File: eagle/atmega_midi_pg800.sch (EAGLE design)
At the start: 39 parts, among them IC1 78L05Z, IC2 4067N, IC3 4067N, IC4 4067N, Q1 16.000Mhz, U1 6N138, U2 ATMEGA328P_PDIP, X1 MAB6H

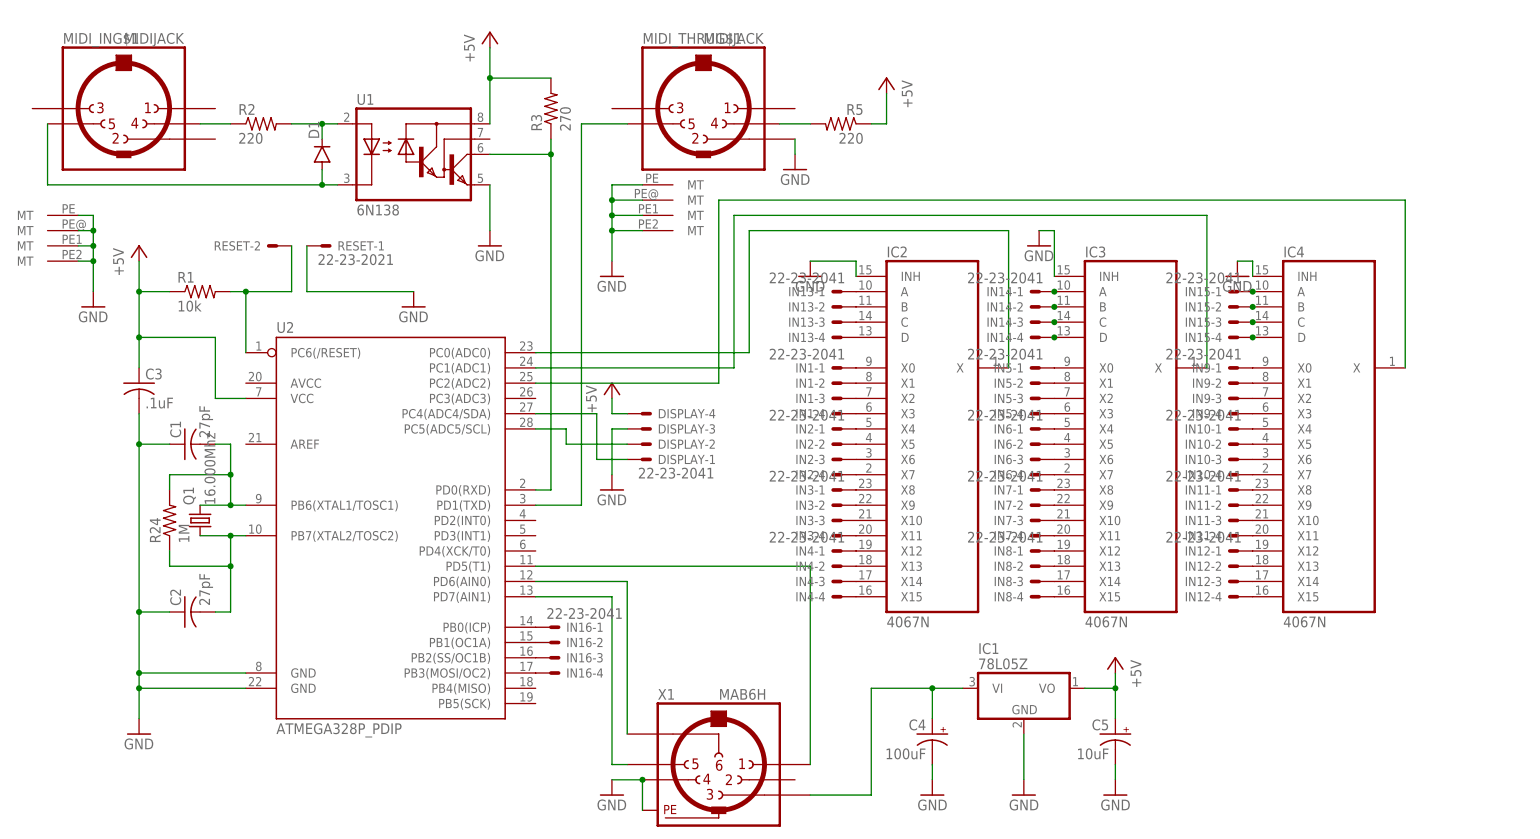
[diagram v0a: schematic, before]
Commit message: rotary encoder connection
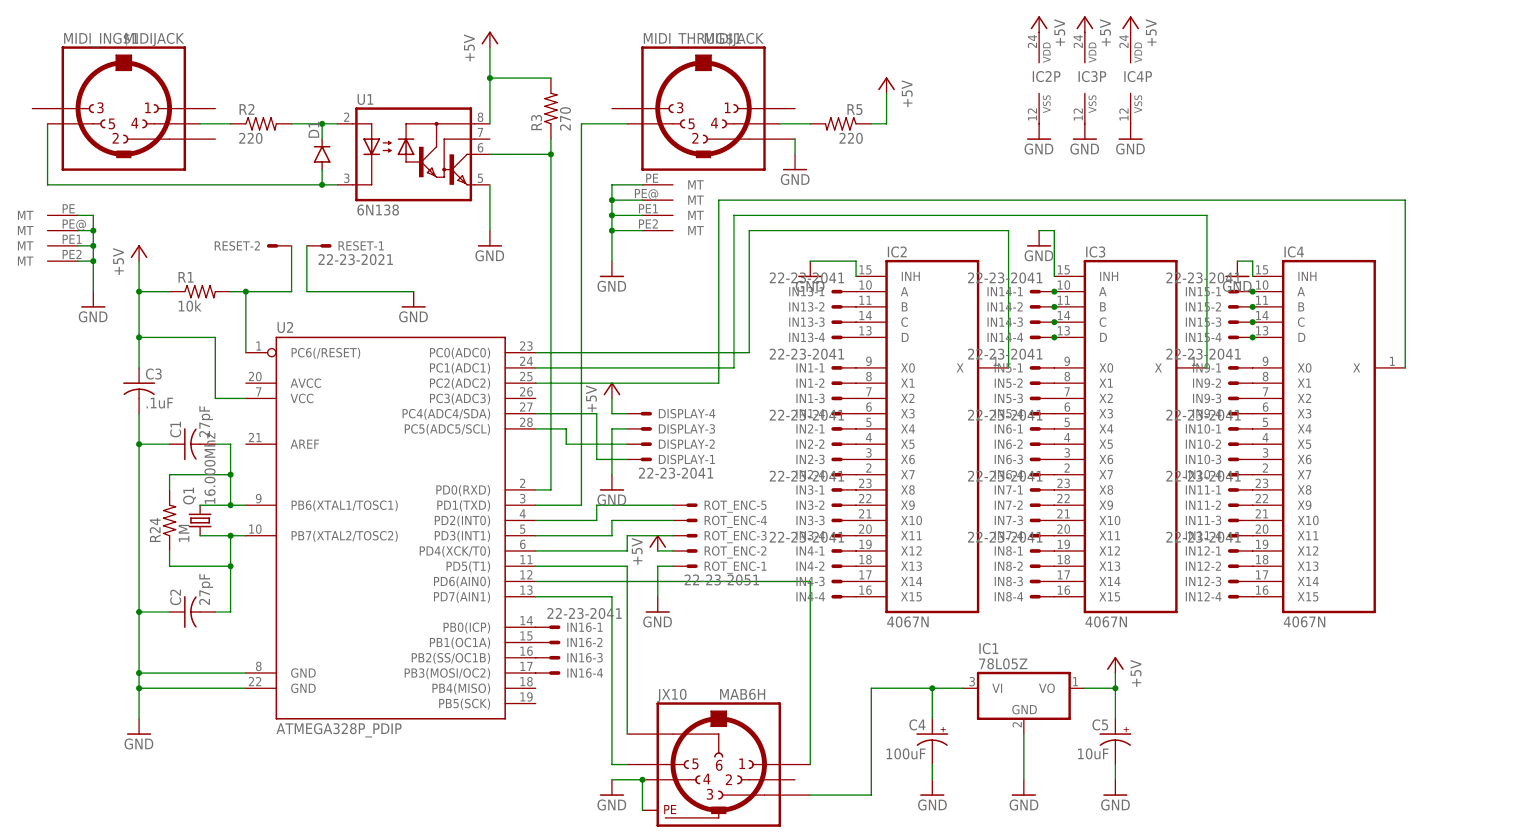
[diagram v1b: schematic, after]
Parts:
- added ROT_ENC: 22-23-2051, con-molex:22-23-2051
- R5: device rcl:R-US_0207/10 -> rcl:R-US_0309/10
- renumbered X1 to JX10
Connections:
- new net N$84: ROT_ENC-5.S, U2.PD2(INT0)
- new net N$85: ROT_ENC-4.S, U2.PD3(INT1)
- new net N$86: ROT_ENC-3.S, U2.PD4(XCK/T0)
- net +5V: now also IC2P.VDD, IC3P.VDD, IC4P.VDD, ROT_ENC-2.S
- net GND: now also IC2P.VSS, IC3P.VSS, IC4P.VSS, ROT_ENC-1.S
- net N$10: now also U2.PD6(AIN0); no longer U2.PD5(T1)
- net N$9: now also U2.PD5(T1); no longer U2.PD6(AIN0)

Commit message: big boy version of 7805 to power those 4067 and the display
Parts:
- removed IC1: 78L05Z, linear:78L05Z
- added IC5: 7805TV, linear:7805TV
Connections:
- net +5V: now also IC5.VO; no longer IC1.VO
- net GND: now also IC5.GND; no longer IC1.GND
- net N$6: now also IC5.VI; no longer IC1.VI
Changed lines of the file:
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@@
 <part name="GND1" library="supply1" deviceset="GND" device=""/>
 <part name="JX10" library="con-hirschmann" deviceset="MAB6H" device=""/>
-<part name="IC1" library="linear" deviceset="78*" device="Z" technology="L05"/>
 <part name="GND3" library="supply1" deviceset="GND" device=""/>
 <part name="C4" library="rcl" deviceset="CPOL-US" device="B45181A" value="100uF"/>
@@
 <part name="GND18" library="supply1" deviceset="GND" device=""/>
 <part name="P+9" library="supply1" deviceset="+5V" device=""/>
+<part name="IC5" library="linear" deviceset="78*" device="TV" technology="05"/>
 </parts>
 <sheets>
@@
 <instance part="GND1" gate="1" x="53.34" y="86.36"/>
 <instance part="JX10" gate="G$1" x="71.12" y="5.08"/>
-<instance part="IC1" gate="A1" x="121.92" y="17.78"/>
 <instance part="GND3" gate="1" x="53.34" y="0"/>
 <instance part="C4" gate="G$1" x="106.68" y="10.16" rot="MR0"/>
@@
 <instance part="GND18" gate="1" x="60.96" y="30.48"/>
 <instance part="P+9" gate="1" x="60.96" y="43.18"/>
+<instance part="IC5" gate="A1" x="121.92" y="17.78"/>
 </instances>
 <busses>
@@
 </segment>
 <segment>
-<pinref part="IC1" gate="A1" pin="VO"/>
 <pinref part="C5" gate="G$1" pin="+"/>
 <wire x1="132.08" y1="17.78" x2="137.16" y2="17.78" width="0.1524" layer="91"/>
@@
 <wire x1="137.16" y1="20.32" x2="137.16" y2="17.78" width="0.1524" layer="91"/>
 <junction x="137.16" y="17.78"/>
+<pinref part="IC5" gate="A1" pin="VO"/>
 </segment>
 <segment>
@@
 </segment>
 <segment>
-<pinref part="IC1" gate="A1" pin="GND"/>
 <wire x1="121.92" y1="2.54" x2="121.92" y2="10.16" width="0.1524" layer="91"/>
 <pinref part="GND15" gate="1" pin="GND"/>
+<pinref part="IC5" gate="A1" pin="GND"/>
 </segment>
 <segment>
@@
 <net name="N$6" class="0">
 <segment>
-<pinref part="IC1" gate="A1" pin="VI"/>
 <pinref part="C4" gate="G$1" pin="+"/>
 <wire x1="106.68" y1="17.78" x2="111.76" y2="17.78" width="0.1524" layer="91"/>
@@
 <wire x1="96.52" y1="17.78" x2="96.52" y2="0" width="0.1524" layer="91"/>
 <wire x1="96.52" y1="0" x2="86.36" y2="0" width="0.1524" layer="91"/>
-</segment>
-</net>
+<pinref part="IC5" gate="A1" pin="VI"/>
+</segment>
+</net>

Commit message: protectoin diode and pot power hookups
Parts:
- added D2: 1N4004, diode:1N4004
- added POT_PWR, POT_PWR1, POT_PWR2: 22-23-2021, con-molex:22-23-2021
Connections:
- net +5V: now also D2.A, POT_PWR-2.S, POT_PWR1-2.S, POT_PWR2-2.S
- net GND: now also POT_PWR-1.S, POT_PWR1-1.S, POT_PWR2-1.S
- net N$6: now also D2.C
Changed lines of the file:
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@@
 <?xml version="1.0" encoding="utf-8"?>
 <!DOCTYPE eagle SYSTEM "eagle.dtd">
-<eagle version="7.6.0">
+<eagle version="7.7.0">
 <drawing>
 <settings>
@@
 <grid distance="0.1" unitdist="inch" unit="inch" style="lines" multiple="1" display="no" altdistance="0.01" altunitdist="inch" altunit="inch"/>
 <layers>
-<layer number="1" name="Top" color="4" fill="1" visible="yes" active="no"/>
-<layer number="16" name="Bottom" color="1" fill="1" visible="yes" active="no"/>
-<layer number="17" name="Pads" color="2" fill="1" visible="yes" active="no"/>
-<layer number="18" name="Vias" color="2" fill="1" visible="yes" active="no"/>
-<layer number="19" name="Unrouted" color="6" fill="1" visible="yes" active="no"/>
-<layer number="20" name="Dimension" color="15" fill="1" visible="yes" active="no"/>
-<layer number="21" name="tPlace" color="7" fill="1" visible="yes" active="no"/>
-<layer number="22" name="bPlace" color="7" fill="1" visible="yes" active="no"/>
-<layer number="23" name="tOrigins" color="15" fill="1" visible="yes" active="no"/>
-<layer number="24" name="bOrigins" color="15" fill="1" visible="yes" active="no"/>
-<layer number="25" name="tNames" color="7" fill="1" visible="yes" active="no"/>
-<layer number="26" name="bNames" color="7" fill="1" visible="yes" active="no"/>
-<layer number="27" name="tValues" color="7" fill="1" visible="yes" active="no"/>
-<layer number="28" name="bValues" color="7" fill="1" visible="yes" active="no"/>
+<layer number="1" name="Top" color="4" fill="1" visible="no" active="no"/>
+<layer number="16" name="Bottom" color="1" fill="1" visible="no" active="no"/>
+<layer number="17" name="Pads" color="2" fill="1" visible="no" active="no"/>
+<layer number="18" name="Vias" color="2" fill="1" visible="no" active="no"/>
+<layer number="19" name="Unrouted" color="6" fill="1" visible="no" active="no"/>
+<layer number="20" name="Dimension" color="15" fill="1" visible="no" active="no"/>
+<layer number="21" name="tPlace" color="7" fill="1" visible="no" active="no"/>
+<layer number="22" name="bPlace" color="7" fill="1" visible="no" active="no"/>
+<layer number="23" name="tOrigins" color="15" fill="1" visible="no" active="no"/>
+<layer number="24" name="bOrigins" color="15" fill="1" visible="no" active="no"/>
+<layer number="25" name="tNames" color="7" fill="1" visible="no" active="no"/>
+<layer number="26" name="bNames" color="7" fill="1" visible="no" active="no"/>
+<layer number="27" name="tValues" color="7" fill="1" visible="no" active="no"/>
+<layer number="28" name="bValues" color="7" fill="1" visible="no" active="no"/>
 <layer number="29" name="tStop" color="7" fill="3" visible="no" active="no"/>
 <layer number="30" name="bStop" color="7" fill="6" visible="no" active="no"/>
@@
 <layer number="35" name="tGlue" color="7" fill="4" visible="no" active="no"/>
 <layer number="36" name="bGlue" color="7" fill="5" visible="no" active="no"/>
-<layer number="37" name="tTest" color="7" fill="1" visible="yes" active="no"/>
-<layer number="38" name="bTest" color="7" fill="1" visible="yes" active="no"/>
+<layer number="37" name="tTest" color="7" fill="1" visible="no" active="no"/>
+<layer number="38" name="bTest" color="7" fill="1" visible="no" active="no"/>
 <layer number="39" name="tKeepout" color="4" fill="11" visible="no" active="no"/>
 <layer number="40" name="bKeepout" color="1" fill="11" visible="no" active="no"/>
@@
 <layer number="44" name="Drills" color="7" fill="1" visible="no" active="no"/>
 <layer number="45" name="Holes" color="7" fill="1" visible="no" active="no"/>
-<layer number="46" name="Milling" color="3" fill="1" visible="yes" active="no"/>
-<layer number="47" name="Measures" color="7" fill="1" visible="yes" active="no"/>
-<layer number="48" name="Document" color="7" fill="1" visible="yes" active="no"/>
-<layer number="49" name="Reference" color="7" fill="1" visible="yes" active="no"/>
-<layer number="50" name="dxf" color="7" fill="1" visible="yes" active="no"/>
-<layer number="51" name="tDocu" color="7" fill="1" visible="yes" active="no"/>
-<layer number="52" name="bDocu" color="7" fill="1" visible="yes" active="no"/>
-<layer number="53" name="tGND_GNDA" color="7" fill="9" visible="yes" active="no"/>
-<layer number="54" name="bGND_GNDA" color="1" fill="9" visible="yes" active="no"/>
-<layer number="56" name="wert" color="7" fill="1" visible="yes" active="no"/>
-<layer number="57" name="tCAD" color="7" fill="1" visible="yes" active="no"/>
-<layer number="59" name="tCarbon" color="7" fill="1" visible="yes" active="no"/>
-<layer number="60" name="bCarbon" color="7" fill="1" visible="yes" active="no"/>
+<layer number="46" name="Milling" color="3" fill="1" visible="no" active="no"/>
+<layer number="47" name="Measures" color="7" fill="1" visible="no" active="no"/>
+<layer number="48" name="Document" color="7" fill="1" visible="no" active="no"/>
+<layer number="49" name="Reference" color="7" fill="1" visible="no" active="no"/>
+<layer number="50" name="dxf" color="7" fill="1" visible="no" active="no"/>
+<layer number="51" name="tDocu" color="7" fill="1" visible="no" active="no"/>
+<layer number="52" name="bDocu" color="7" fill="1" visible="no" active="no"/>
+<layer number="53" name="tGND_GNDA" color="7" fill="9" visible="no" active="no"/>
+<layer number="54" name="bGND_GNDA" color="1" fill="9" visible="no" active="no"/>
+<layer number="56" name="wert" color="7" fill="1" visible="no" active="no"/>
+<layer number="57" name="tCAD" color="7" fill="1" visible="no" active="no"/>
+<layer number="59" name="tCarbon" color="7" fill="1" visible="no" active="no"/>
+<layer number="60" name="bCarbon" color="7" fill="1" visible="no" active="no"/>
 <layer number="90" name="Modules" color="5" fill="1" visible="yes" active="yes"/>
 <layer number="91" name="Nets" color="2" fill="1" visible="yes" active="yes"/>
@@
 <part name="P+9" library="supply1" deviceset="+5V" device=""/>
 <part name="IC5" library="linear" deviceset="78*" device="TV" technology="05"/>
+<part name="POT_PWR" library="con-molex" deviceset="22-23-2021" device=""/>
+<part name="D2" library="diode" deviceset="1N4004" device=""/>
+<part name="POT_PWR1" library="con-molex" deviceset="22-23-2021" device=""/>
+<part name="POT_PWR2" library="con-molex" deviceset="22-23-2021" device=""/>
+<part name="P+10" library="supply1" deviceset="+5V" device=""/>
+<part name="P+11" library="supply1" deviceset="+5V" device=""/>
+<part name="P+12" library="supply1" deviceset="+5V" device=""/>
+<part name="GND19" library="supply1" deviceset="GND" device=""/>
+<part name="GND20" library="supply1" deviceset="GND" device=""/>
+<part name="GND21" library="supply1" deviceset="GND" device=""/>
 </parts>
 <sheets>
@@
 <instance part="P+9" gate="1" x="60.96" y="43.18"/>
 <instance part="IC5" gate="A1" x="121.92" y="17.78"/>
+<instance part="POT_PWR" gate="-1" x="167.64" y="12.7" rot="MR180"/>
+<instance part="POT_PWR" gate="-2" x="167.64" y="15.24" rot="MR180"/>
+<instance part="D2" gate="1" x="121.92" y="25.4" rot="R180"/>
+<instance part="POT_PWR1" gate="-1" x="167.64" y="2.54" rot="MR180"/>
+<instance part="POT_PWR1" gate="-2" x="167.64" y="5.08" rot="MR180"/>
+<instance part="POT_PWR2" gate="-1" x="187.96" y="12.7" rot="MR180"/>
+<instance part="POT_PWR2" gate="-2" x="187.96" y="15.24" rot="MR180"/>
+<instance part="P+10" gate="1" x="165.1" y="17.78" rot="MR0"/>
+<instance part="P+11" gate="1" x="165.1" y="7.62" rot="MR0"/>
+<instance part="P+12" gate="1" x="185.42" y="17.78" rot="MR0"/>
+<instance part="GND19" gate="1" x="165.1" y="0" rot="MR0"/>
+<instance part="GND20" gate="1" x="165.1" y="10.16" rot="MR0"/>
+<instance part="GND21" gate="1" x="185.42" y="10.16" rot="MR0"/>
 </instances>
 <busses>
@@
 <segment>
 <pinref part="C5" gate="G$1" pin="+"/>
-<wire x1="132.08" y1="17.78" x2="137.16" y2="17.78" width="0.1524" layer="91"/>
+<wire x1="132.08" y1="17.78" x2="134.62" y2="17.78" width="0.1524" layer="91"/>
+<wire x1="134.62" y1="17.78" x2="137.16" y2="17.78" width="0.1524" layer="91"/>
 <wire x1="137.16" y1="17.78" x2="137.16" y2="12.7" width="0.1524" layer="91"/>
 <pinref part="P+4" gate="1" pin="+5V"/>
@@
 <junction x="137.16" y="17.78"/>
 <pinref part="IC5" gate="A1" pin="VO"/>
+<wire x1="124.46" y1="25.4" x2="134.62" y2="25.4" width="0.1524" layer="91"/>
+<wire x1="134.62" y1="25.4" x2="134.62" y2="17.78" width="0.1524" layer="91"/>
+<junction x="134.62" y="17.78"/>
+<pinref part="D2" gate="1" pin="A"/>
 </segment>
 <segment>
@@
 <pinref part="ROT_ENC" gate="-2" pin="S"/>
 <wire x1="60.96" y1="40.64" x2="63.5" y2="40.64" width="0.1524" layer="91"/>
+</segment>
+<segment>
+<pinref part="POT_PWR" gate="-2" pin="S"/>
+<pinref part="P+10" gate="1" pin="+5V"/>
+</segment>
+<segment>
+<pinref part="POT_PWR1" gate="-2" pin="S"/>
+<pinref part="P+11" gate="1" pin="+5V"/>
+</segment>
+<segment>
+<pinref part="POT_PWR2" gate="-2" pin="S"/>
+<pinref part="P+12" gate="1" pin="+5V"/>
 </segment>
 </net>
@@
 <wire x1="60.96" y1="38.1" x2="63.5" y2="38.1" width="0.1524" layer="91"/>
 </segment>
+<segment>
+<pinref part="POT_PWR1" gate="-1" pin="S"/>
+<pinref part="GND19" gate="1" pin="GND"/>
+</segment>
+<segment>
+<pinref part="POT_PWR" gate="-1" pin="S"/>
+<pinref part="GND20" gate="1" pin="GND"/>
+</segment>
+<segment>
+<pinref part="POT_PWR2" gate="-1" pin="S"/>
+<pinref part="GND21" gate="1" pin="GND"/>
+</segment>
 </net>
 <net name="N$42" class="0">
@@
 <wire x1="96.52" y1="0" x2="86.36" y2="0" width="0.1524" layer="91"/>
 <pinref part="IC5" gate="A1" pin="VI"/>
-</segment>
-</net>
+<pinref part="D2" gate="1" pin="C"/>
+<wire x1="119.38" y1="25.4" x2="106.68" y2="25.4" width="0.1524" layer="91"/>
+<wire x1="106.68" y1="25.4" x2="106.68" y2="17.78" width="0.1524" layer="91"/>
+</segment>
+</net>
